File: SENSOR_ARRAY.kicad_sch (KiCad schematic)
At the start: 40 parts, among them IC1 TBD62083AFNG_Z,EL_, IC2 74HC238D,653, IC5 CD4051BM_TR, IC6 CD4051BM_TR, J3 FH34SRJ-8S-0.5SH_50_, Q1 MMBT3904, U1 QRE1113GR, U10 QRE1113GR, U11 QRE1113GR, U12 QRE1113GR, U13 QRE1113GR, U14 QRE1113GR, U15 QRE1113GR, U16 QRE1113GR, U2 QRE1113GR, U3 QRE1113GR, U4 QRE1113GR, U5 QRE1113GR, U6 QRE1113GR, U7 QRE1113GR, U8 QRE1113GR, U9 QRE1113GR

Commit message: Changed motor driver from DRV8874 to a simpler, small-footprint DRV8837 using the IN1/IN2 interface.
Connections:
- net +3.3V: no longer C1.1, C2.1, IC2.16 (VCC), IC5.16 (VDD), IC6.16 (VDD), J3.8, RC1.2, RC2.2, REN2.2
- new net VCC: C1.1, C2.1, IC2.16 (VCC), IC5.16 (VDD), IC6.16 (VDD), J3.8, RC1.2, RC2.2, REN2.2
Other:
- moved on the sheet: RC1, RC2

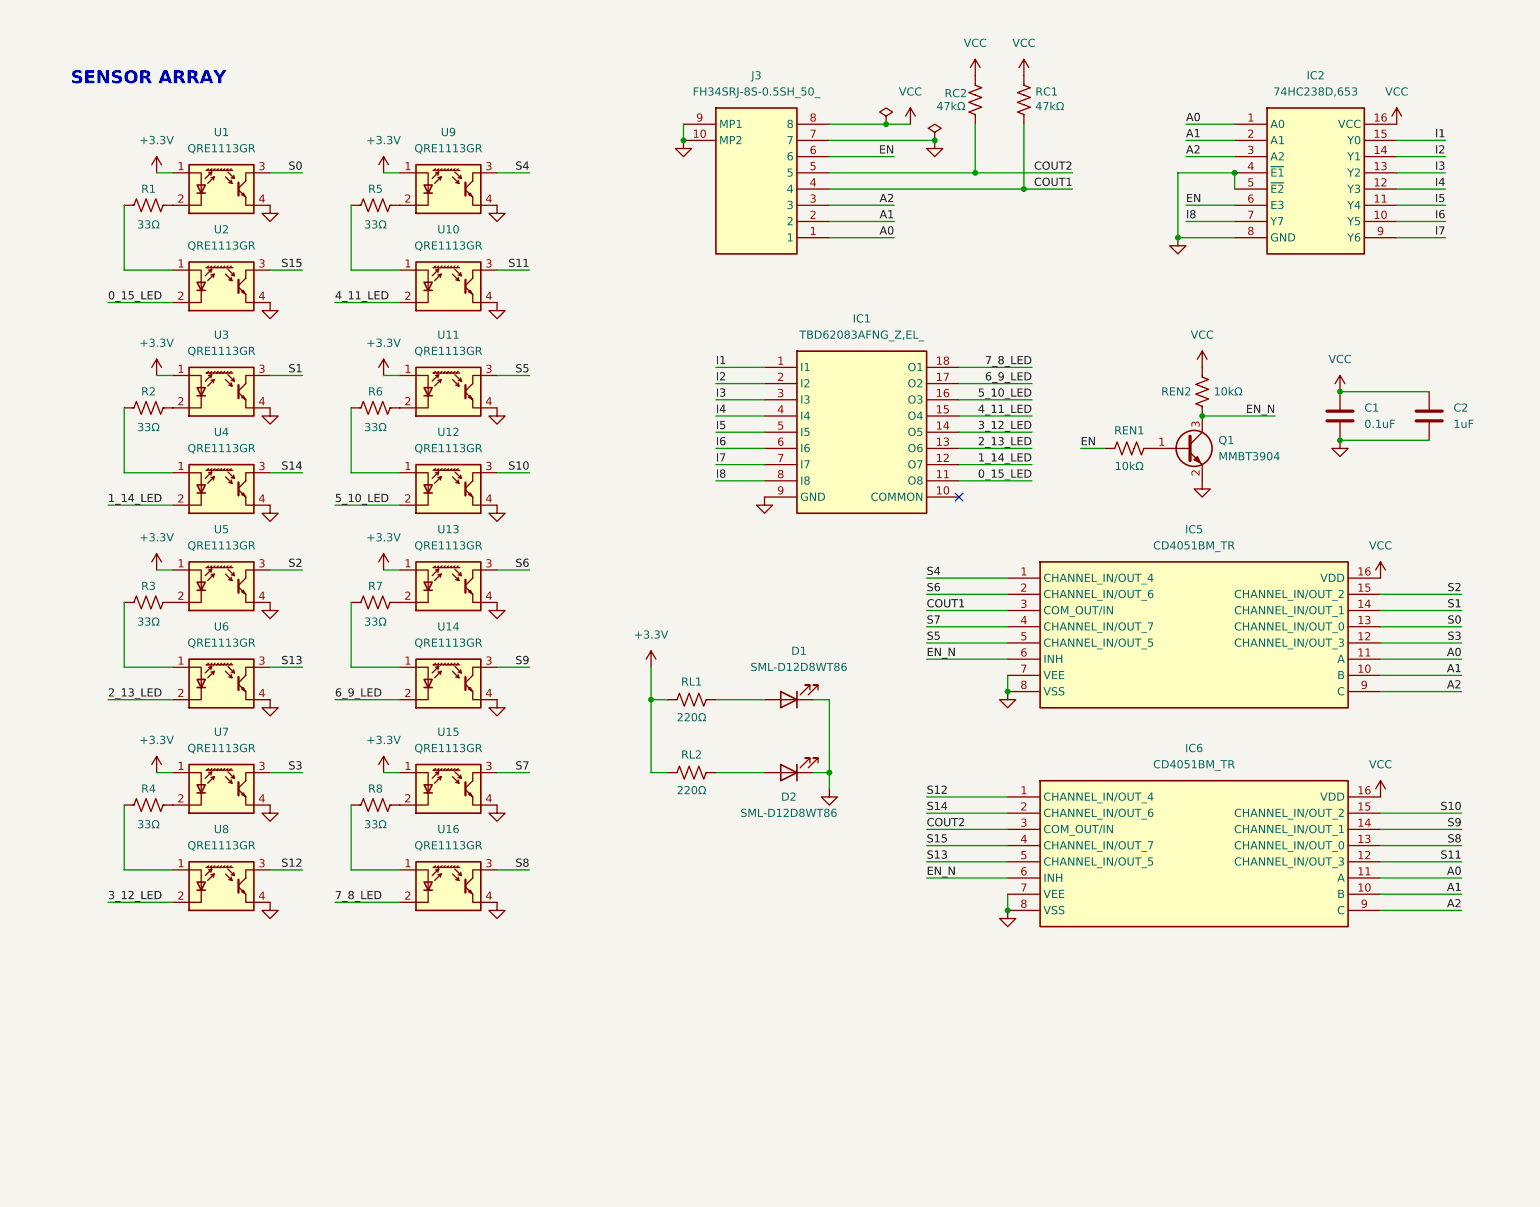
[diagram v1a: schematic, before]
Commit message: Added ESP32-C3-MINI-1 circuit for the PD control over AP STA. Added comments and read sequence explanation. The schematic is finished, please add tag.
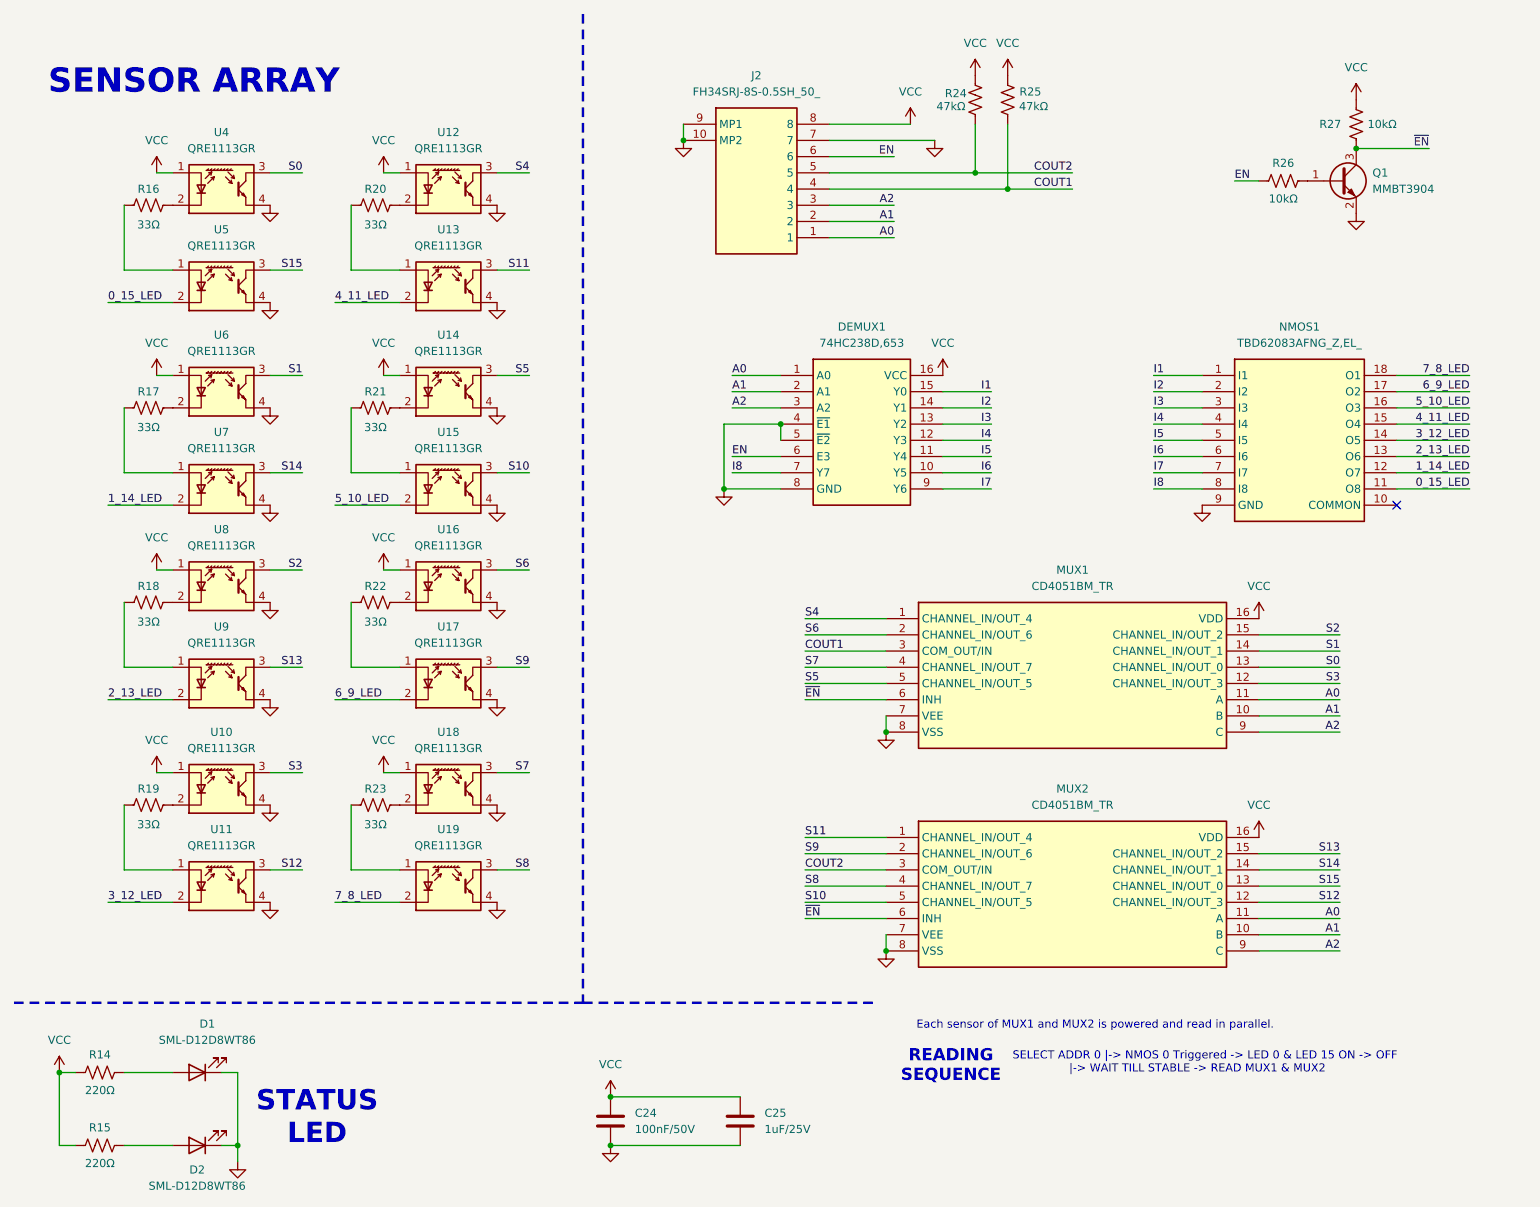
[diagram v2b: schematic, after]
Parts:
- C24: renamed from C1; value 0.1uF -> 100nF/50V
- C25: renamed from C2; value 1uF -> 1uF/25V
- renumbered IC2 to DEMUX1, J3 to J2, IC5 to MUX1, IC6 to MUX2, IC1 to NMOS1, RL1 to R14, RL2 to R15, R1 to R16, R2 to R17, R3 to R18, R4 to R19, R5 to R20, R6 to R21, R7 to R22, R8 to R23, RC2 to R24, RC1 to R25, REN1 to R26, REN2 to R27, U7 to U10, U8 to U11, U9 to U12, U10 to U13, U11 to U14, U12 to U15, U13 to U16, U14 to U17, U15 to U18, U16 to U19, U1 to U4, U2 to U5, U3 to U6, U4 to U7, U5 to U8, U6 to U9
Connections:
- net +3.3V is gone; now on net VCC: R14.1, R15.1, U10.1 (A), U12.1 (A), U14.1 (A), U16.1 (A), U18.1 (A), U4.1 (A), U6.1 (A), U8.1 (A)
- net S10: now also MUX2.5 (CHANNEL_IN/OUT_5); no longer MUX2.15 (CHANNEL_IN/OUT_2)
- net S11: now also MUX2.1 (CHANNEL_IN/OUT_4); no longer MUX2.12 (CHANNEL_IN/OUT_3)
- net S12: now also MUX2.12 (CHANNEL_IN/OUT_3); no longer MUX2.1 (CHANNEL_IN/OUT_4)
- net S13: now also MUX2.15 (CHANNEL_IN/OUT_2); no longer MUX2.5 (CHANNEL_IN/OUT_5)
- net S14: now also MUX2.14 (CHANNEL_IN/OUT_1); no longer MUX2.2 (CHANNEL_IN/OUT_6)
- net S15: now also MUX2.13 (CHANNEL_IN/OUT_0); no longer MUX2.4 (CHANNEL_IN/OUT_7)
- net S8: now also MUX2.4 (CHANNEL_IN/OUT_7); no longer MUX2.13 (CHANNEL_IN/OUT_0)
- net S9: now also MUX2.2 (CHANNEL_IN/OUT_6); no longer MUX2.14 (CHANNEL_IN/OUT_1)
- net EN_N renamed ~{EN}
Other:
- note added: "Each sensor of MUX1 and MUX2 is powered and read in parallel."
- note added: "READING SEQUENCE"
- note added: "SELECT ADDR 0 |-> NMOS 0 Triggered -> LED 0 & LED 15 ON -> OFF |-> WAIT TILL STABLE -> READ MUX1 & MUX2"
- note added: "STATUS LED"
- moved on the sheet: C24, C25, D1, D2, DEMUX1, MUX1, MUX2, NMOS1, Q1, R14, R15, R25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

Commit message: Added dedicated Current Sensing IC INA240. Changed Buck output from 3.8V (edge of Teensy's LDO supply voltage) to 5V.
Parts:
- renumbered C24 to C31, C25 to C32

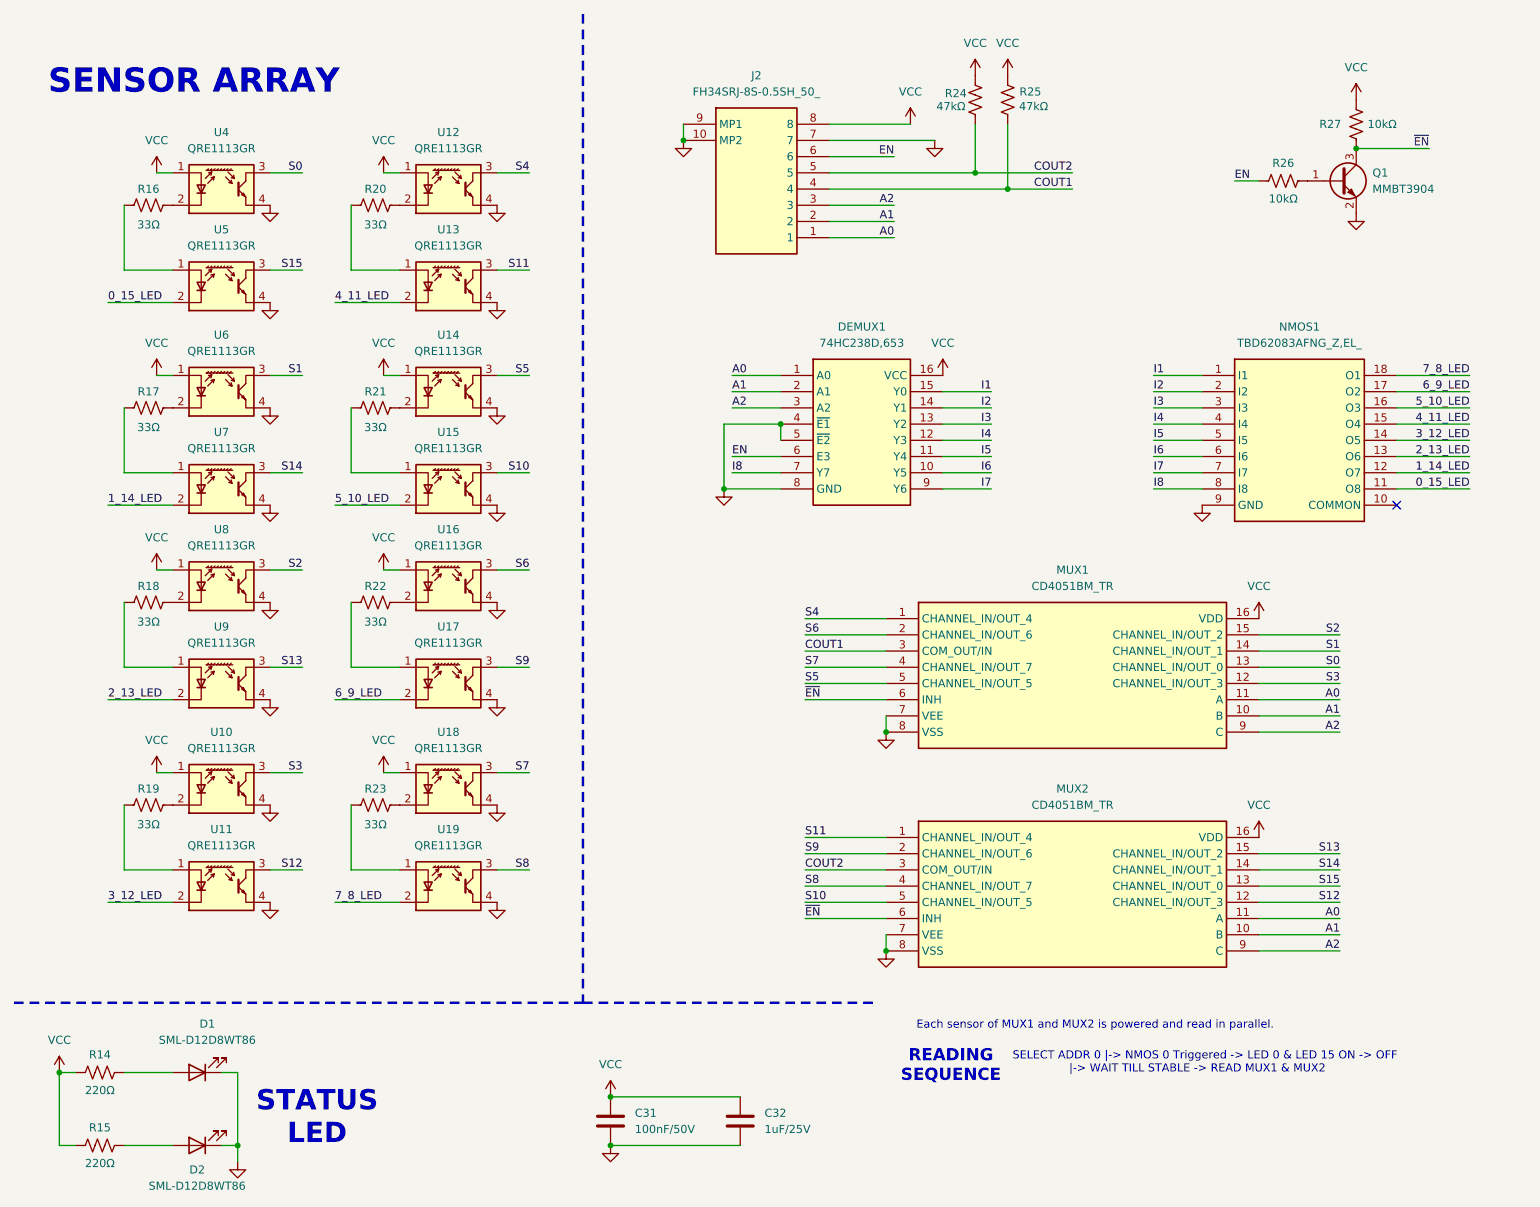
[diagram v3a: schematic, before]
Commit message: Added decoupling for sensor board. Changed the relatively old CD4051BM with over 400 ohm to 74HC4051. Added for the first time hierarchical label to connect the FFC pins across schematics.
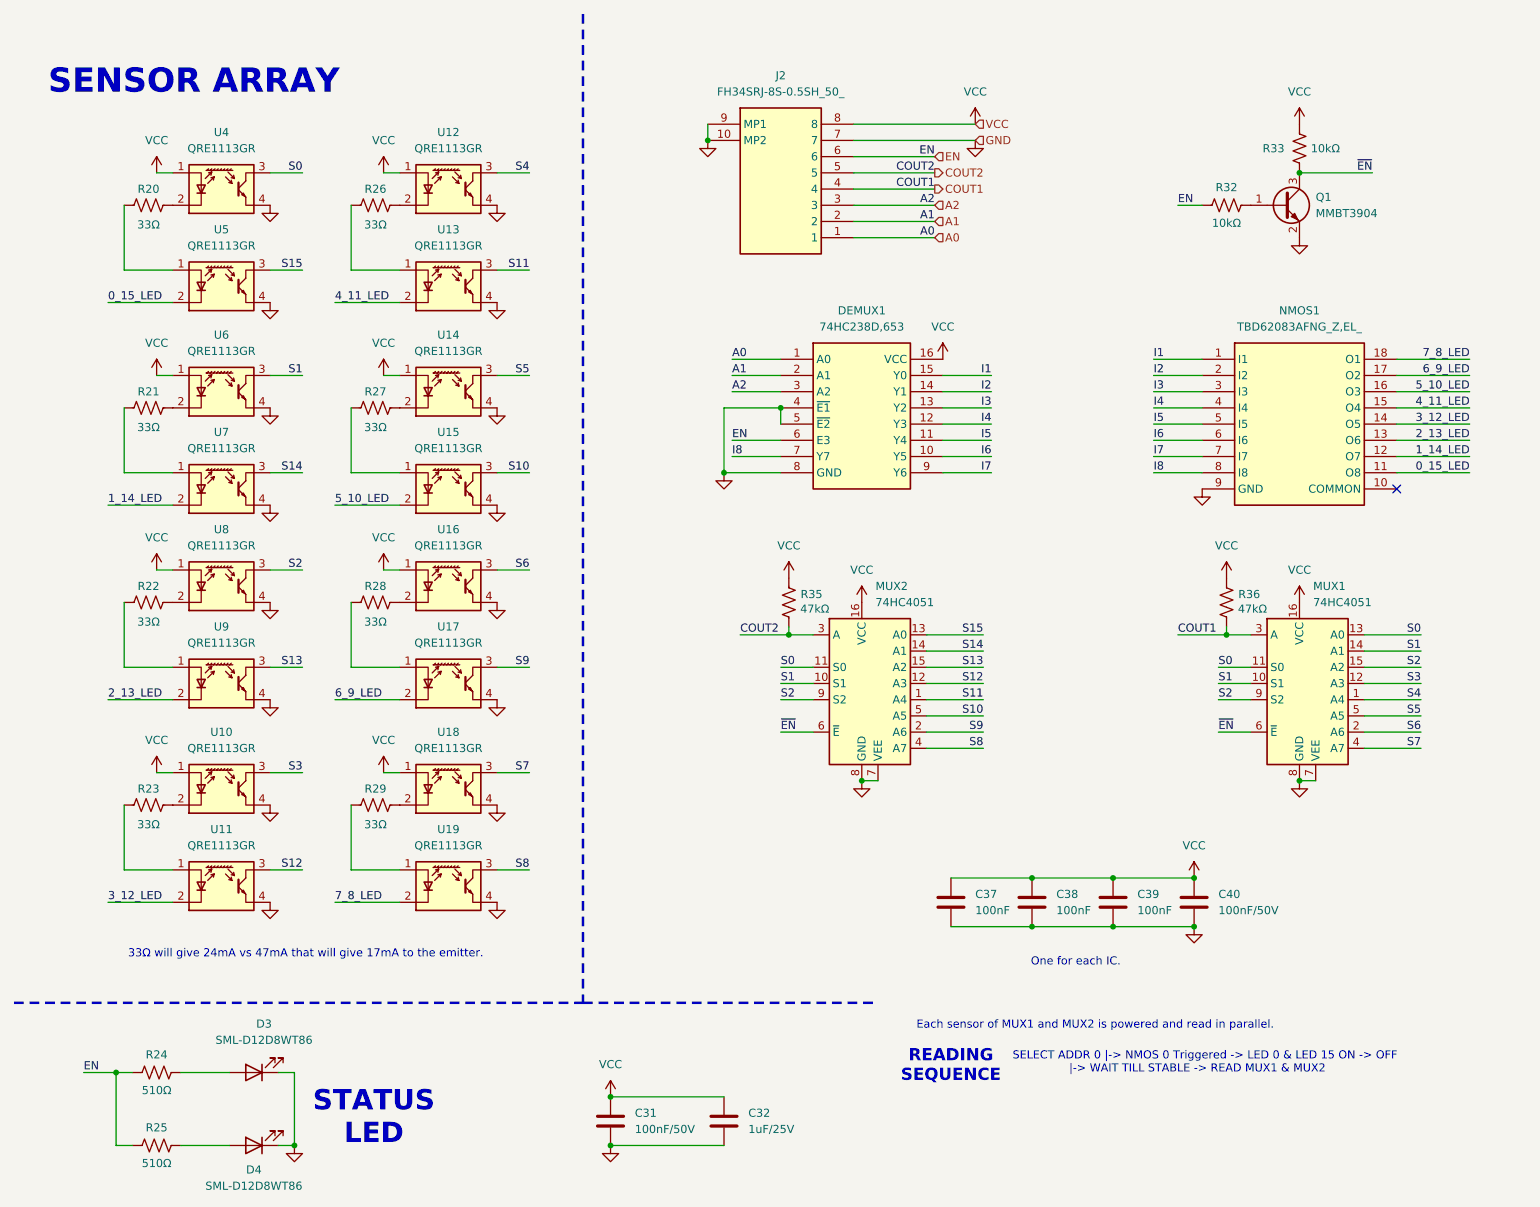
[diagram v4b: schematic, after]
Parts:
- removed MUX1, MUX2: CD4051BM_TR, SAVITAR:SOIC127P602X182-16N, symbol SAVITAR:CD4051BM_TR
- removed R14, R15: 220Ω, Resistor_SMD:R_0603_1608Metric_Pad0.98x0.95mm_HandSolder, symbol Device:R_US
- added C37, C38, C39: 100nF, Capacitor_SMD:C_0603_1608Metric, symbol Device:C
- added C40: 100nF/50V, Capacitor_SMD:C_0603_1608Metric, symbol Device:C
- added MUX1, MUX2: 74HC4051, Package_SO:SOIC-16_3.9x9.9mm_P1.27mm, symbol 74xx:74HC4051
- added R35, R36: 47kΩ, Resistor_SMD:R_0603_1608Metric, symbol Device:R_US
- C31, C32: footprint Capacitor_SMD:C_0603_1608Metric_Pad1.08x0.95mm_HandSolder -> Capacitor_SMD:C_0603_1608Metric
- D3: renamed from D1; footprint LED_SMD:LED_0603_1608Metric_Pad1.05x0.95mm_HandSolder -> LED_SMD:LED_0603_1608Metric
- D4: renamed from D2; footprint LED_SMD:LED_0603_1608Metric_Pad1.05x0.95mm_HandSolder -> LED_SMD:LED_0603_1608Metric
- R20: renamed from R16; footprint Resistor_SMD:R_0603_1608Metric_Pad0.98x0.95mm_HandSolder -> Resistor_SMD:R_0603_1608Metric
- R21: renamed from R17; footprint Resistor_SMD:R_0603_1608Metric_Pad0.98x0.95mm_HandSolder -> Resistor_SMD:R_0603_1608Metric
- R22: renamed from R18; footprint Resistor_SMD:R_0603_1608Metric_Pad0.98x0.95mm_HandSolder -> Resistor_SMD:R_0603_1608Metric
- R23: renamed from R19; footprint Resistor_SMD:R_0603_1608Metric_Pad0.98x0.95mm_HandSolder -> Resistor_SMD:R_0603_1608Metric
- R24, R25: value 47kΩ -> 510Ω; footprint Resistor_SMD:R_0603_1608Metric_Pad0.98x0.95mm_HandSolder -> Resistor_SMD:R_0603_1608Metric
- R26: renamed from R20; footprint Resistor_SMD:R_0603_1608Metric_Pad0.98x0.95mm_HandSolder -> Resistor_SMD:R_0603_1608Metric
- R27: renamed from R21; footprint Resistor_SMD:R_0603_1608Metric_Pad0.98x0.95mm_HandSolder -> Resistor_SMD:R_0603_1608Metric
- R28: renamed from R22; footprint Resistor_SMD:R_0603_1608Metric_Pad0.98x0.95mm_HandSolder -> Resistor_SMD:R_0603_1608Metric
- R29: renamed from R23; footprint Resistor_SMD:R_0603_1608Metric_Pad0.98x0.95mm_HandSolder -> Resistor_SMD:R_0603_1608Metric
- R32: renamed from R26; footprint Resistor_SMD:R_0603_1608Metric_Pad0.98x0.95mm_HandSolder -> Resistor_SMD:R_0603_1608Metric
- R33: renamed from R27; footprint Resistor_SMD:R_0603_1608Metric_Pad0.98x0.95mm_HandSolder -> Resistor_SMD:R_0603_1608Metric
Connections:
- net COUT1: now also MUX1.3 (A), R36.1; no longer R25.1
- net COUT2: now also MUX2.3 (A), R35.1; no longer R24.1
- net EN: now also R24.1, R25.1
- net GND: now also C37.2, C38.2, C39.2, C40.2, MUX1.7 (VEE), MUX1.8 (GND), MUX2.7 (VEE), MUX2.8 (GND)
- net S0: now also MUX1.11 (S0), MUX1.13 (A0), MUX2.11 (S0)
- net S1: now also MUX1.10 (S1), MUX1.14 (A1), MUX2.10 (S1)
- net S10: now also MUX2.5 (A5)
- net S11: now also MUX2.1 (A4)
- net S12: now also MUX2.12 (A3)
- net S13: now also MUX2.15 (A2)
- net S14: now also MUX2.14 (A1)
- net S15: now also MUX2.13 (A0)
- net S2: now also MUX1.15 (A2), MUX1.9 (S2), MUX2.9 (S2)
- net S3: now also MUX1.12 (A3)
- net S4: now also MUX1.1 (A4)
- net S5: now also MUX1.5 (A5)
- net S6: now also MUX1.2 (A6)
- net S7: now also MUX1.4 (A7)
- net S8: now also MUX2.4 (A7)
- net S9: now also MUX2.2 (A6)
- net VCC: now also C37.1, C38.1, C39.1, C40.1, MUX1.16 (VCC), MUX2.16 (VCC), R35.2, R36.2; no longer R24.2, R25.2
- net ~{EN}: now also MUX1.6 (~{E}), MUX2.6 (~{E})
- net at D4.2 (A): now also R25.2
- net at D3.2 (A): now also R24.2
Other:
- note added: "33Ω will give 24mA vs 47mA that will give 17mA to the emitter."
- note added: "One for each IC."
- moved on the sheet: C32, D3, D4, DEMUX1, J2, NMOS1, Q1, R32, R33
